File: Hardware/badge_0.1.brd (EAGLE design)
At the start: 100 x 50 mm, 62 parts, among them CON1 PH_2, IC1 CP2102, IC2 PIMH9, J7 2X6 FEMALE, SW2 MK12C02, U4 MCP73832T-2DCI/OT

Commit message: Routing optimizations Less contorted traces Making use of unused space for routing
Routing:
- net GND: track 378.8 -> 387.3 mm, vias 121 -> 120
- net CH_PD: track 40.9 -> 39.5 mm
- net TX: track 88.4 -> 89.8 mm
- net 5V: track 70.1 -> 71.3 mm, vias 4 -> 2

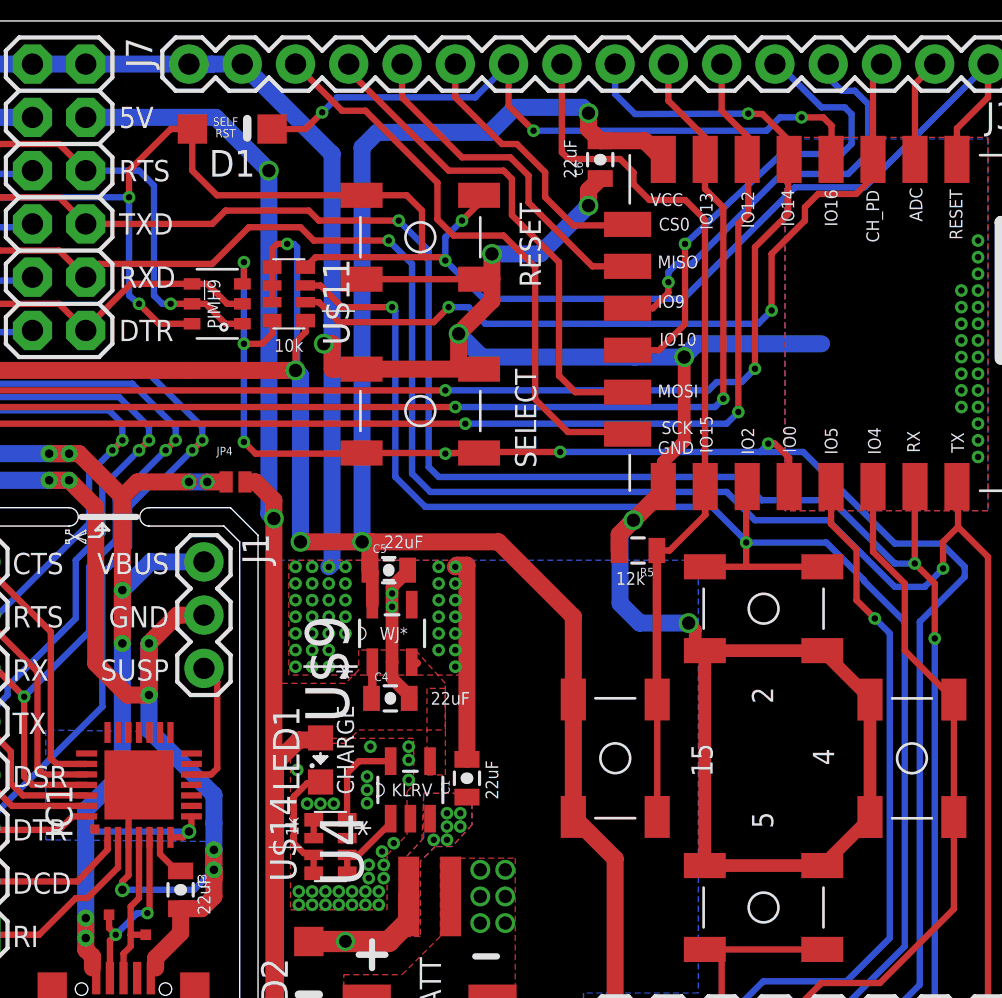
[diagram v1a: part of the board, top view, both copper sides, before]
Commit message: Added deep-sleep jumper point (closed by default); More routing optimizations
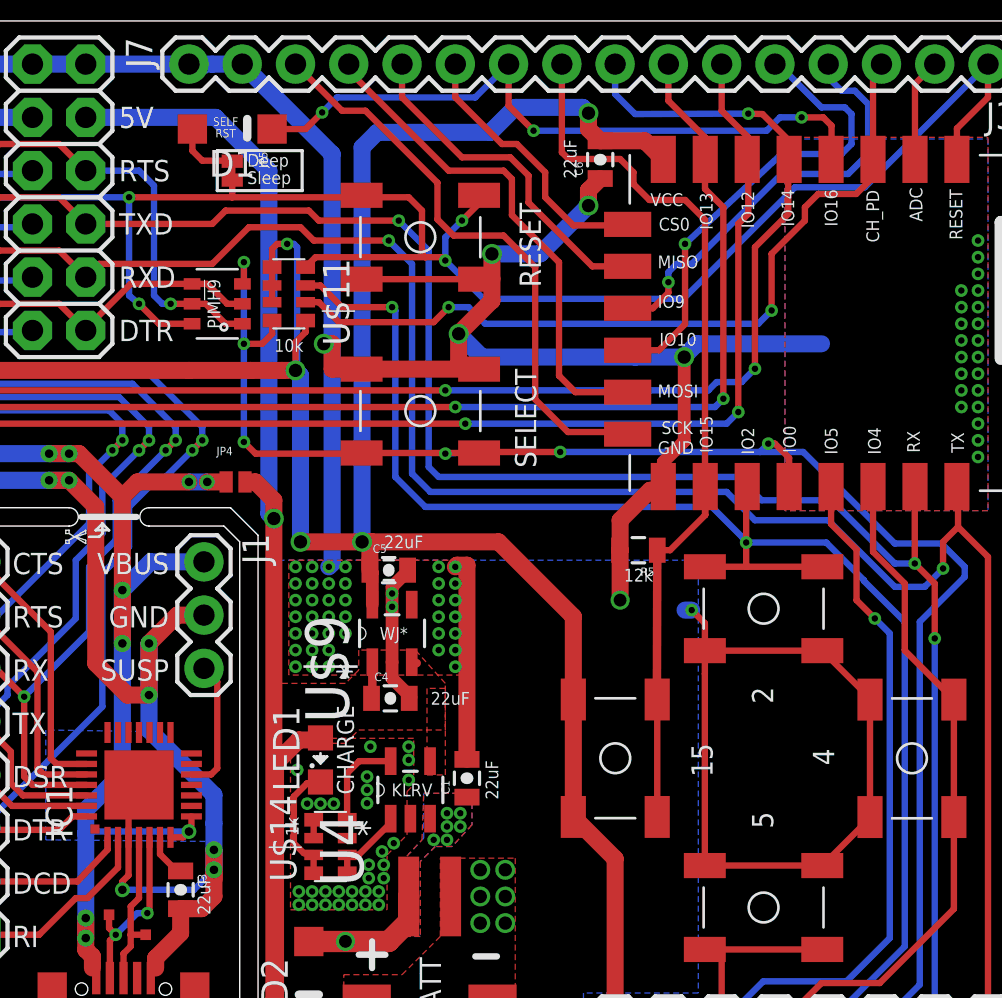
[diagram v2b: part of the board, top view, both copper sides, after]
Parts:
- added JP5: JUMPER-PAD-2-NOJELLY, SparkFun-Passives:JELLYPAD-JUMPER-2-NO_NO_SILK
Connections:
- net RESET: now also JP5.1, JP5.2
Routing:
- net GND: track 387.3 -> 382.8 mm
- net 5V: vias 2 -> 1
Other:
- board text added: "Deep Sleep"

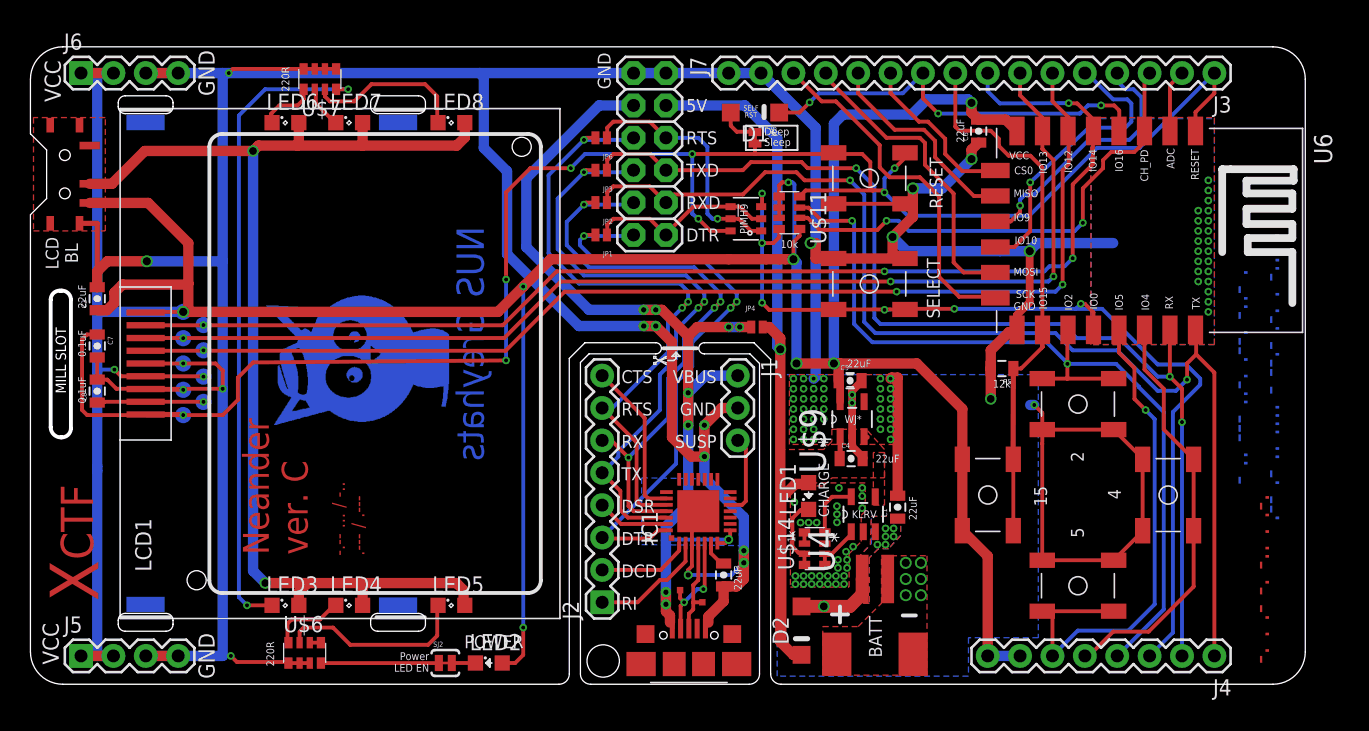
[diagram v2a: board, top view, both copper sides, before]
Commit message: Expanded the power supply area upwards, made all caps same dir
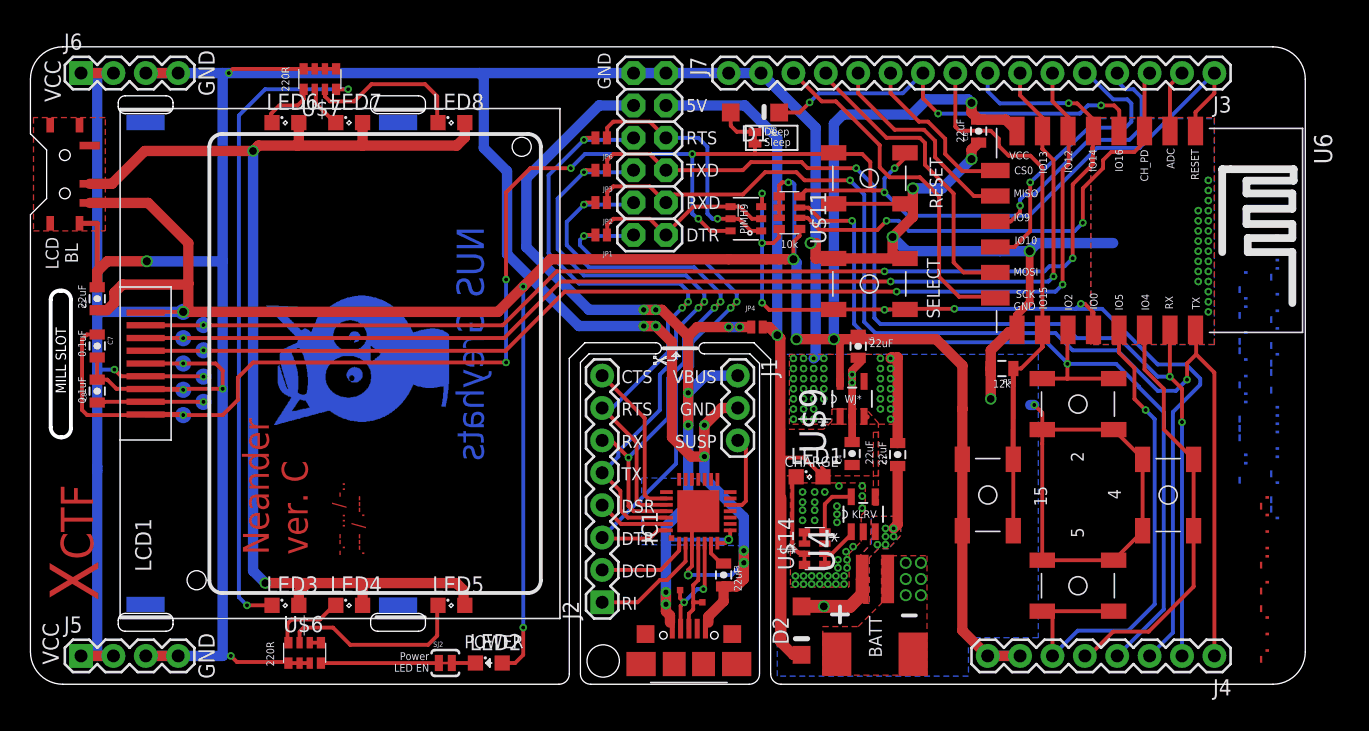
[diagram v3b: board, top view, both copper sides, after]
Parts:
- moved C1 4.13 mm to (68.0, 18.0)
- moved C5 2.77 mm to (64.9, 26.5), turned to 270 degrees
- moved U$9 1.59 mm to (64.5, 22.4)
- moved LED1 1.51 mm to (61.1, 16.3), turned to 0 degrees
- moved C4 0.40 mm to (64.5, 18.1), turned to 90 degrees
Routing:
- net VBAT: track 6.35 -> 11.4 mm
- net GND: track 382.8 -> 378.5 mm, vias 120 -> 125
- net N$1: track 6.01 -> 8.42 mm
- net VCC: track 276.3 -> 278.2 mm
- net 5V: track 71.3 -> 72.6 mm
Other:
- board text removed: "SELF RST"

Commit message: electrons still dropped out for some strange reason
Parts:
- moved C1 0.08 mm to (68.0, 18.1)
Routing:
- net GPIO15/SPI_CS: track 44.2 -> 42.9 mm
- net GND: track 378.5 -> 377.8 mm
- net VCC: track 278.2 -> 277.6 mm
- net N$1: track 8.42 -> 7.89 mm
- net GPIO0: track 76.1 -> 75.6 mm, vias 6 -> 5

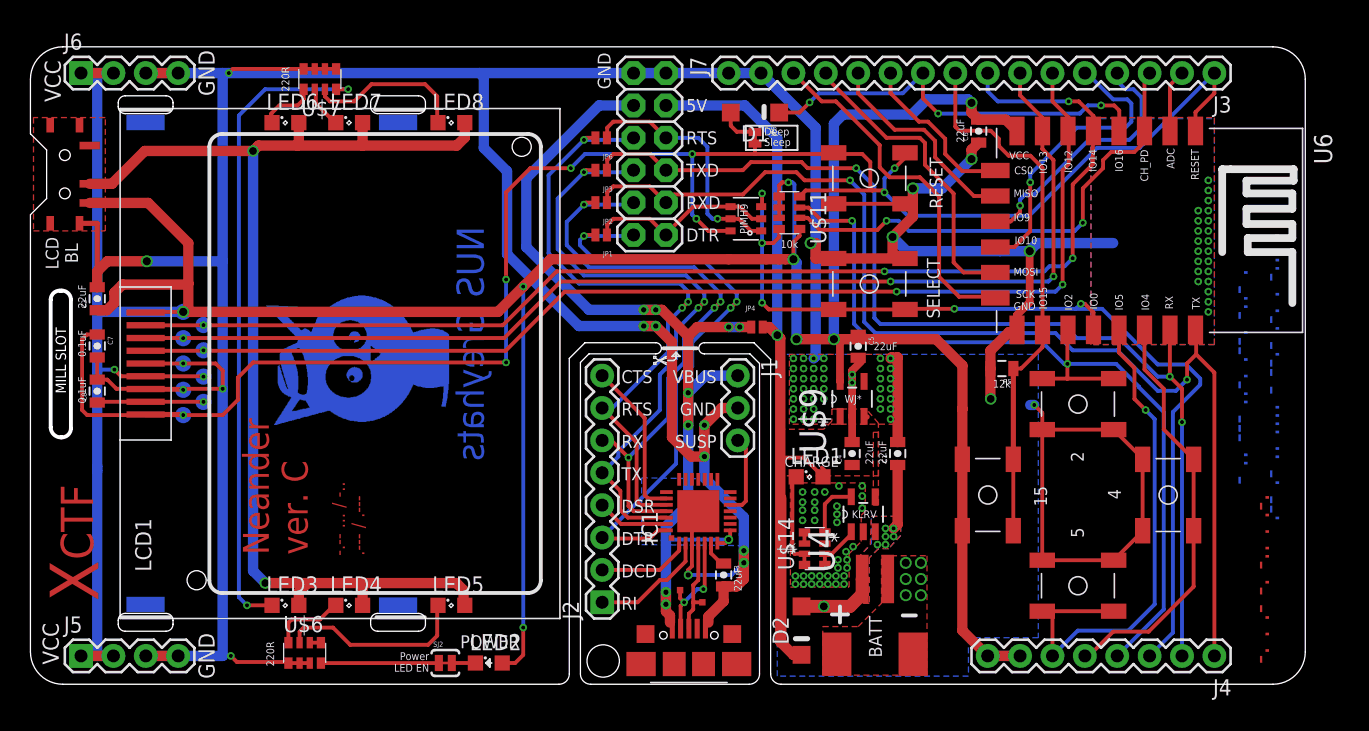
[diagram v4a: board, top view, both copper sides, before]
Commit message: made slot wider for lanyard
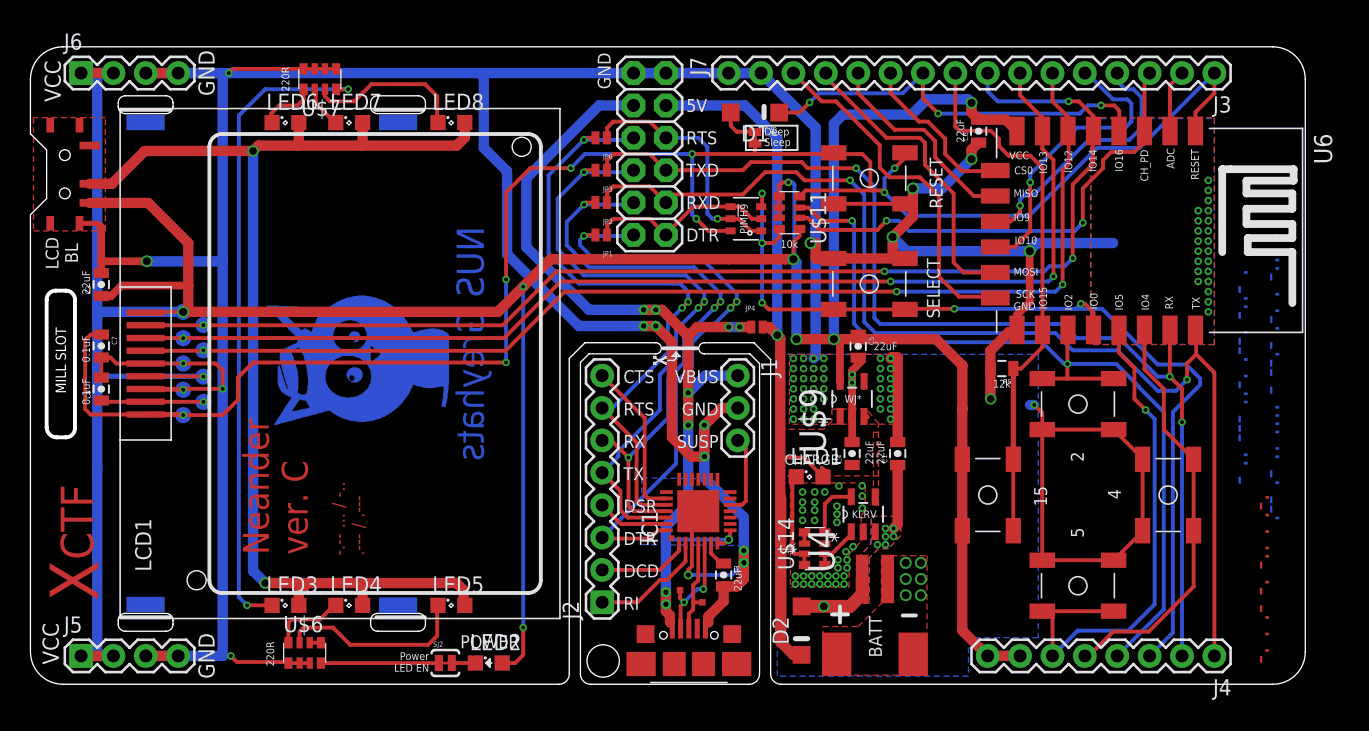
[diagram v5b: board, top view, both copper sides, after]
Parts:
- moved C2 1.16 mm to (5.56, 31.4)
- moved C9 0.35 mm to (5.56, 23.2)
- moved C7 0.32 mm to (5.56, 26.5)
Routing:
- net GND: track 377.8 -> 374.4 mm
- net VCC: track 277.6 -> 280.7 mm, vias 10 -> 9
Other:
- outline, holes or cut-outs redrawn
